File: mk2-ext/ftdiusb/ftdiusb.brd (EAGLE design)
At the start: 30.5 x 55.9 mm, 23 parts, among them IC1 FT232BL, Q1 6MHz

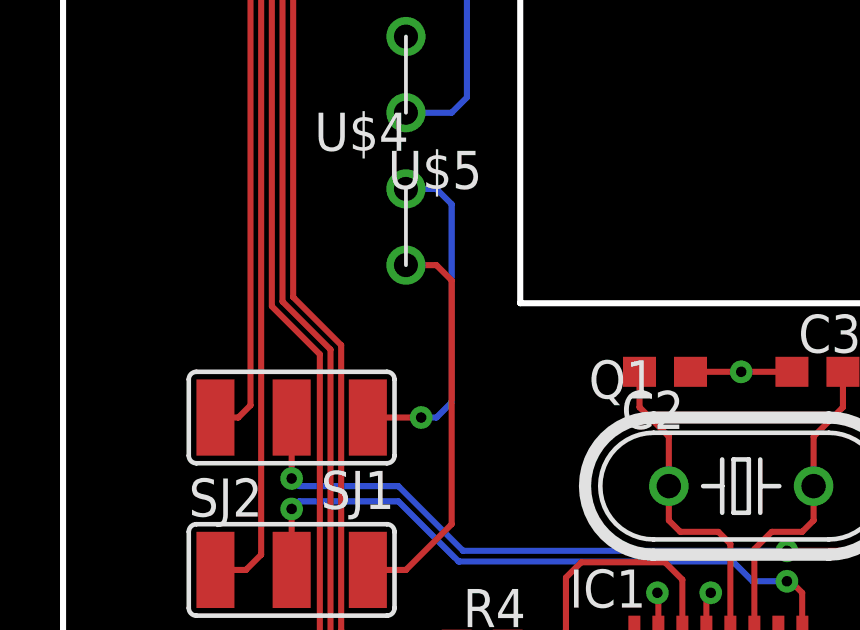
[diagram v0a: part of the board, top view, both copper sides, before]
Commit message: [fix mk2 text size]
	- increase the font size of texts to make the smallest ones readable
	  for the mk2 shield, extension header and ftdiusb extension board
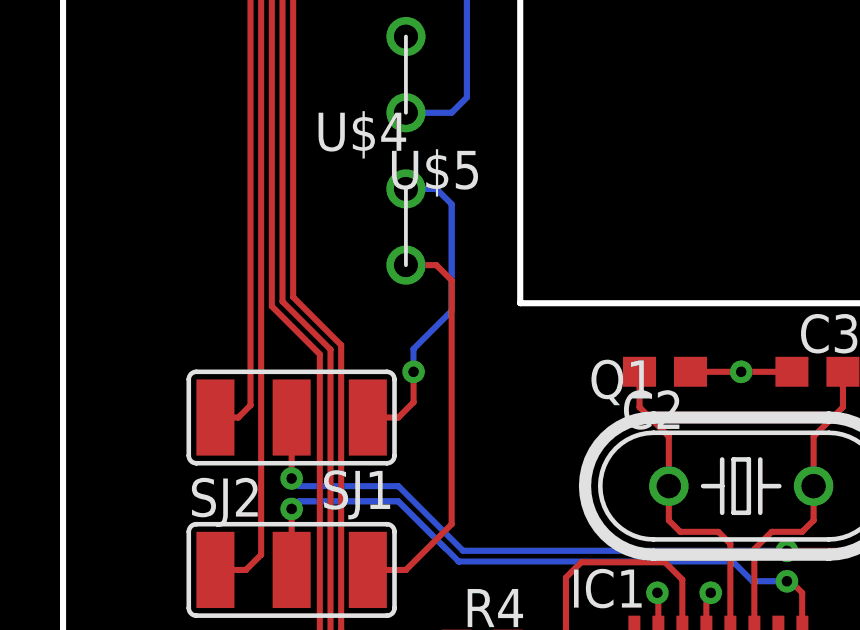
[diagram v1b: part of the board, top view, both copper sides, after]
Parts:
- Q1: value 6MHz -> 6M
- RX, TX: value LED_0603 -> red
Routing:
- net TX1: track 11.3 -> 10.6 mm
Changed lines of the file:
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@@
 <setting verticaltext="up"/>
 </settings>
-<grid distance="50" unitdist="mil" unit="mil" style="lines" multiple="1" display="yes" altdistance="5" altunitdist="mil" altunit="mil"/>
+<grid distance="10" unitdist="mil" unit="mil" style="lines" multiple="1" display="yes" altdistance="5" altunitdist="mil" altunit="mil"/>
 <layers>
 <layer number="1" name="Top" color="4" fill="1" visible="yes" active="yes"/>
-<layer number="16" name="Bottom" color="1" fill="1" visible="no" active="yes"/>
+<layer number="16" name="Bottom" color="1" fill="1" visible="yes" active="yes"/>
 <layer number="17" name="Pads" color="2" fill="1" visible="yes" active="yes"/>
 <layer number="18" name="Vias" color="2" fill="1" visible="yes" active="yes"/>
@@
 <wire x1="26.67" y1="3.81" x2="29.21" y2="6.35" width="0.2032" layer="20"/>
 <wire x1="26.67" y1="59.69" x2="29.21" y2="57.15" width="0.2032" layer="20"/>
-<text x="7.62" y="55.88" size="0.3048" layer="48" align="center-left">TX0</text>
-<text x="7.62" y="53.34" size="0.3048" layer="48" align="center-left">RX0</text>
-<text x="7.62" y="35.56" size="0.3048" layer="48" align="center-left">GND</text>
-<text x="7.62" y="33.02" size="0.3048" layer="48" align="center-left">VCC</text>
-<text x="7.62" y="30.48" size="0.3048" layer="48" align="center-left">TX1</text>
-<text x="7.62" y="27.94" size="0.3048" layer="48" align="center-left">RX1</text>
+<text x="8.128" y="55.88" size="0.6096" layer="48" align="center-right">TX0</text>
+<text x="8.128" y="53.34" size="0.6096" layer="48" align="center-right">RX0</text>
+<text x="8.128" y="35.56" size="0.6096" layer="48" align="center-right">GND</text>
+<text x="8.128" y="33.02" size="0.6096" layer="48" align="center-right">VCC</text>
+<text x="8.128" y="30.48" size="0.6096" layer="48" align="center-right">TX1</text>
+<text x="8.128" y="27.94" size="0.6096" layer="48" align="center-right">RX1</text>
 <wire x1="-1.27" y1="59.69" x2="-1.27" y2="3.81" width="0.2032" layer="20"/>
 <wire x1="29.21" y1="26.67" x2="13.97" y2="26.67" width="0.2032" layer="20"/>
 <wire x1="13.97" y1="26.67" x2="13.97" y2="39.37" width="0.2032" layer="20"/>
 <wire x1="13.97" y1="39.37" x2="29.21" y2="39.37" width="0.2032" layer="20"/>
-<text x="1.27" y="22.86" size="0.6096" layer="48" rot="R90" align="center">TX0</text>
-<text x="1.27" y="17.78" size="0.6096" layer="48" rot="R90" align="center">RX0</text>
-<text x="11.43" y="22.86" size="0.6096" layer="48" rot="R90" align="center">TX1</text>
-<text x="11.43" y="17.78" size="0.6096" layer="48" rot="R90" align="center">RX1</text>
-<text x="10.16" y="6.35" size="0.6096" layer="48" rot="R90" align="center">RX</text>
-<text x="1.27" y="6.35" size="0.6096" layer="48" rot="R90" align="center">TX</text>
-<text x="17.78" y="54.61" size="0.6096" layer="48" rot="R90" align="center">VCC OUT</text>
+<text x="1.778" y="22.86" size="0.8128" layer="48" rot="R90" align="center">TX0</text>
+<text x="1.778" y="17.78" size="0.8128" layer="48" rot="R90" align="center">RX0</text>
+<text x="10.922" y="22.86" size="0.8128" layer="48" rot="R90" align="center">TX1</text>
+<text x="10.922" y="17.78" size="0.8128" layer="48" rot="R90" align="center">RX1</text>
+<text x="10.16" y="6.35" size="0.8128" layer="48" rot="R90" align="center">RX</text>
+<text x="1.27" y="6.35" size="0.8128" layer="48" rot="R90" align="center">TX</text>
+<text x="17.78" y="54.61" size="0.8128" layer="48" rot="R90" align="center">VCC OUT</text>
 </plain>
 <attributes>
@@
 <attribute name="VALUE" x="13.081" y="39.751" size="1.27" layer="27"/>
 </element>
-<element name="Q1" library="crystal" library_urn="urn:adsk.eagle:library:204" package="HC49U-V" package3d_urn="urn:adsk.eagle:package:12075/1" value="6MHz" x="21.336" y="20.574" smashed="yes">
+<element name="Q1" library="crystal" library_urn="urn:adsk.eagle:library:204" package="HC49U-V" package3d_urn="urn:adsk.eagle:package:12075/1" value="6M" x="21.336" y="20.574" smashed="yes">
 <attribute name="MF" value="" x="21.336" y="20.574" size="1.778" layer="27" display="off"/>
 <attribute name="MPN" value="" x="21.336" y="20.574" size="1.778" layer="27" display="off"/>
@@
 <attribute name="VALUE" x="13.081" y="42.291" size="1.27" layer="27"/>
 </element>
-<element name="TX" library="led" package="C0603" value="LED_0603" x="3.81" y="6.35" smashed="yes">
+<element name="TX" library="led" package="C0603" value="red" x="3.81" y="6.35" smashed="yes">
 <attribute name="NAME" x="3.175" y="6.985" size="1.27" layer="25"/>
 <attribute name="VALUE" x="3.175" y="4.445" size="1.27" layer="27"/>
 </element>
-<element name="RX" library="led" package="C0603" value="LED_0603" x="7.62" y="6.35" smashed="yes">
+<element name="RX" library="led" package="C0603" value="red" x="7.62" y="6.35" smashed="yes">
 <attribute name="NAME" x="6.985" y="6.985" size="1.27" layer="25"/>
 <attribute name="VALUE" x="6.985" y="4.445" size="1.27" layer="27"/>
@@
 <contactref element="SJ1" pad="1"/>
 <contactref element="U$4" pad="P$1"/>
-<wire x1="8.89" y1="22.86" x2="10.668" y2="22.86" width="0.2032" layer="1"/>
-<via x="10.668" y="22.86" extent="1-16" drill="0.35"/>
+<wire x1="8.89" y1="22.86" x2="9.906" y2="22.86" width="0.2032" layer="1"/>
+<wire x1="10.414" y1="23.368" x2="9.906" y2="22.86" width="0.2032" layer="1"/>
+<wire x1="10.414" y1="23.368" x2="10.414" y2="24.384" width="0.2032" layer="1"/>
+<via x="10.414" y="24.384" extent="1-16" drill="0.35"/>
 <wire x1="11.684" y1="29.972" x2="11.176" y2="30.48" width="0.2032" layer="16"/>
 <wire x1="11.176" y1="30.48" x2="10.16" y2="30.48" width="0.2032" layer="16"/>
-<wire x1="10.668" y1="22.86" x2="11.176" y2="22.86" width="0.2032" layer="16"/>
-<wire x1="11.176" y1="22.86" x2="11.684" y2="23.368" width="0.2032" layer="16"/>
-<wire x1="11.684" y1="23.368" x2="11.684" y2="29.972" width="0.2032" layer="16"/>
+<wire x1="11.684" y1="26.416" x2="10.414" y2="25.146" width="0.2032" layer="16"/>
+<wire x1="10.414" y1="24.384" x2="10.414" y2="25.146" width="0.2032" layer="16"/>
+<wire x1="11.684" y1="26.416" x2="11.684" y2="29.972" width="0.2032" layer="16"/>
 </signal>
 <signal name="RX1">

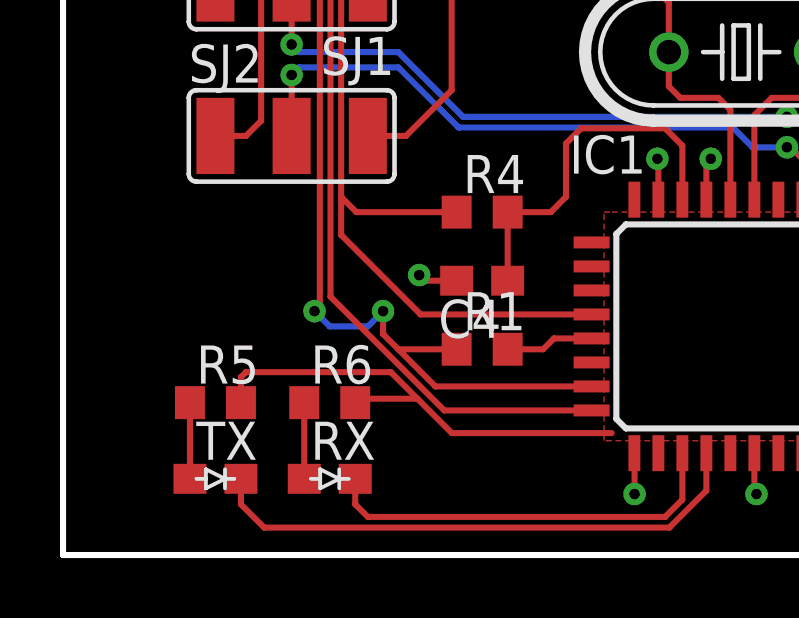
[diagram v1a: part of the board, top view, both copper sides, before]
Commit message: [update fonts]
	- change the size and font of board texts
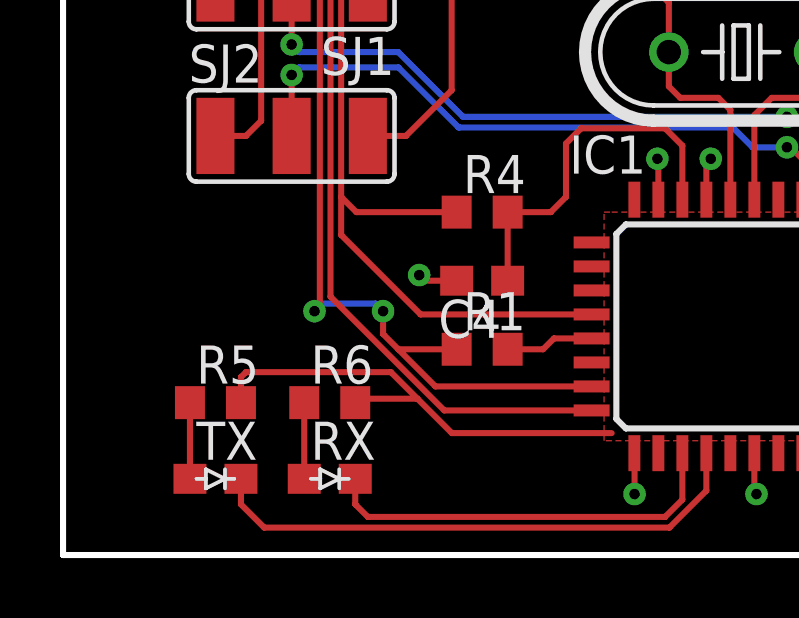
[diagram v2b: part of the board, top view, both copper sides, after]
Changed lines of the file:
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@@
 <wire x1="26.67" y1="3.81" x2="29.21" y2="6.35" width="0.2032" layer="20"/>
 <wire x1="26.67" y1="59.69" x2="29.21" y2="57.15" width="0.2032" layer="20"/>
-<text x="8.128" y="55.88" size="0.6096" layer="48" align="center-right">TX0</text>
-<text x="8.128" y="53.34" size="0.6096" layer="48" align="center-right">RX0</text>
-<text x="8.128" y="35.56" size="0.6096" layer="48" align="center-right">GND</text>
-<text x="8.128" y="33.02" size="0.6096" layer="48" align="center-right">VCC</text>
-<text x="8.128" y="30.48" size="0.6096" layer="48" align="center-right">TX1</text>
-<text x="8.128" y="27.94" size="0.6096" layer="48" align="center-right">RX1</text>
+<text x="8.382" y="55.88" size="0.8128" layer="48" font="fixed" align="center-right">TX0</text>
+<text x="8.382" y="53.34" size="0.8128" layer="48" font="fixed" align="center-right">RX0</text>
+<text x="8.382" y="35.56" size="0.8128" layer="48" font="fixed" align="center-right">GND</text>
+<text x="8.382" y="33.02" size="0.8128" layer="48" font="fixed" align="center-right">VCC</text>
+<text x="8.382" y="30.48" size="0.8128" layer="48" font="fixed" align="center-right">TX1</text>
+<text x="8.382" y="27.94" size="0.8128" layer="48" font="fixed" align="center-right">RX1</text>
 <wire x1="-1.27" y1="59.69" x2="-1.27" y2="3.81" width="0.2032" layer="20"/>
 <wire x1="29.21" y1="26.67" x2="13.97" y2="26.67" width="0.2032" layer="20"/>
 <wire x1="13.97" y1="26.67" x2="13.97" y2="39.37" width="0.2032" layer="20"/>
 <wire x1="13.97" y1="39.37" x2="29.21" y2="39.37" width="0.2032" layer="20"/>
-<text x="1.778" y="22.86" size="0.8128" layer="48" rot="R90" align="center">TX0</text>
-<text x="1.778" y="17.78" size="0.8128" layer="48" rot="R90" align="center">RX0</text>
-<text x="10.922" y="22.86" size="0.8128" layer="48" rot="R90" align="center">TX1</text>
-<text x="10.922" y="17.78" size="0.8128" layer="48" rot="R90" align="center">RX1</text>
-<text x="10.16" y="6.35" size="0.8128" layer="48" rot="R90" align="center">RX</text>
-<text x="1.27" y="6.35" size="0.8128" layer="48" rot="R90" align="center">TX</text>
-<text x="17.78" y="54.61" size="0.8128" layer="48" rot="R90" align="center">VCC OUT</text>
+<text x="1.778" y="22.86" size="1.016" layer="48" font="fixed" rot="R90" align="center">TX0</text>
+<text x="1.778" y="17.78" size="1.016" layer="48" font="fixed" rot="R90" align="center">RX0</text>
+<text x="10.922" y="22.86" size="1.016" layer="48" font="fixed" rot="R90" align="center">TX1</text>
+<text x="10.922" y="17.78" size="1.016" layer="48" font="fixed" rot="R90" align="center">RX1</text>
+<text x="10.16" y="6.35" size="1.016" layer="48" font="fixed" rot="R90" align="center">RX</text>
+<text x="1.27" y="6.35" size="1.016" layer="48" font="fixed" rot="R90" align="center">TX</text>
+<text x="17.78" y="54.61" size="1.016" layer="48" font="fixed" rot="R90" align="center">VCC OUT</text>
 </plain>
 <attributes>
@@
 <wire x1="7.2898" y1="12.1158" x2="7.112" y2="11.938" width="0.2032" layer="1"/>
 <via x="7.112" y="11.938" extent="1-16" drill="0.35"/>
-<wire x1="7.112" y1="11.938" x2="7.62" y2="11.43" width="0.2032" layer="16"/>
-<wire x1="8.89" y1="11.43" x2="9.398" y2="11.938" width="0.2032" layer="16"/>
 <via x="9.398" y="11.938" extent="1-16" drill="0.35"/>
 <wire x1="11.144" y1="9.43" x2="9.906" y2="10.668" width="0.2032" layer="1"/>
@@
 <wire x1="9.398" y1="11.176" x2="9.398" y2="11.938" width="0.2032" layer="1"/>
 <wire x1="7.2898" y1="24.9682" x2="7.2898" y2="12.1158" width="0.2032" layer="1"/>
-<wire x1="7.62" y1="11.43" x2="8.89" y2="11.43" width="0.2032" layer="16"/>
+<wire x1="9.398" y1="11.938" x2="9.144" y2="12.192" width="0.2032" layer="16"/>
+<wire x1="7.112" y1="11.938" x2="7.366" y2="12.192" width="0.2032" layer="16"/>
+<wire x1="9.144" y1="12.192" x2="7.366" y2="12.192" width="0.2032" layer="16"/>
 <wire x1="11.85" y1="10.668" x2="9.906" y2="10.668" width="0.2032" layer="1"/>
 </signal>
